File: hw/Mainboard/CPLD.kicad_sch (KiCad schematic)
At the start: 47 parts, among them J21 FPGA-P4, J22 Conn_02x15_Odd_Even, J23 FPGA_P2, J24 FPGA_P3, Q4 MMBT3904, SW5 CONFIG, U21 T8Q144C3, X1 50MHZ

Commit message: hw: wip
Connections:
- net ~{FPGA_PROG}: now reaches J22.22 (Pin_22)
- no-connect marks 31 -> 30
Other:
- note added: "AD7"
- note added: "~{FPGA_PROG} transitions low during CRESET (before ~{SS}) and returns high after ~{SS} deasserts."
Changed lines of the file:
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@@
   (no_connect (at 151.13 86.36))
   (no_connect (at 457.2 67.31))
-  (no_connect (at 457.2 64.77))
   (no_connect (at 457.2 87.63))
   (no_connect (at 457.2 85.09))
@@
     (stroke (width 0) (type default) (color 0 0 0 0))
   )
+  (wire (pts (xy 421.64 64.77) (xy 457.2 64.77))
+    (stroke (width 0) (type default) (color 0 0 0 0))
+  )
   (bus (pts (xy 337.82 54.61) (xy 337.82 57.15))
     (stroke (width 0) (type default) (color 0 0 0 0))
@@
   )
   (text "NSTATUS driven low on error" (at 435.61 163.83 0)
+    (effects (font (size 1.27 1.27)) (justify left bottom))
+  )
+  (text "~{FPGA_PROG} transitions low during CRESET\n(before ~{SS}) and returns high after ~{SS}\ndeasserts.\n"
+    (at 483.87 55.88 0)
     (effects (font (size 1.27 1.27)) (justify left bottom))
   )
@@
     (effects (font (size 1.27 1.27)) (justify right bottom))
   )
+  (text "AD7" (at 457.2 64.77 180)
+    (effects (font (size 1.27 1.27)) (justify right bottom))
+  )
   (text "BD3" (at 457.2 54.61 180)
     (effects (font (size 1.27 1.27)) (justify right bottom))
@@
     (effects (font (size 1.27 1.27)) (justify left))
   )
+  (hierarchical_label "~{FPGA_PROG}" (shape output) (at 421.64 64.77 180)
+    (effects (font (size 1.27 1.27)) (justify right))
+  )
   (hierarchical_label "VERT" (shape output) (at 386.08 105.41 90)

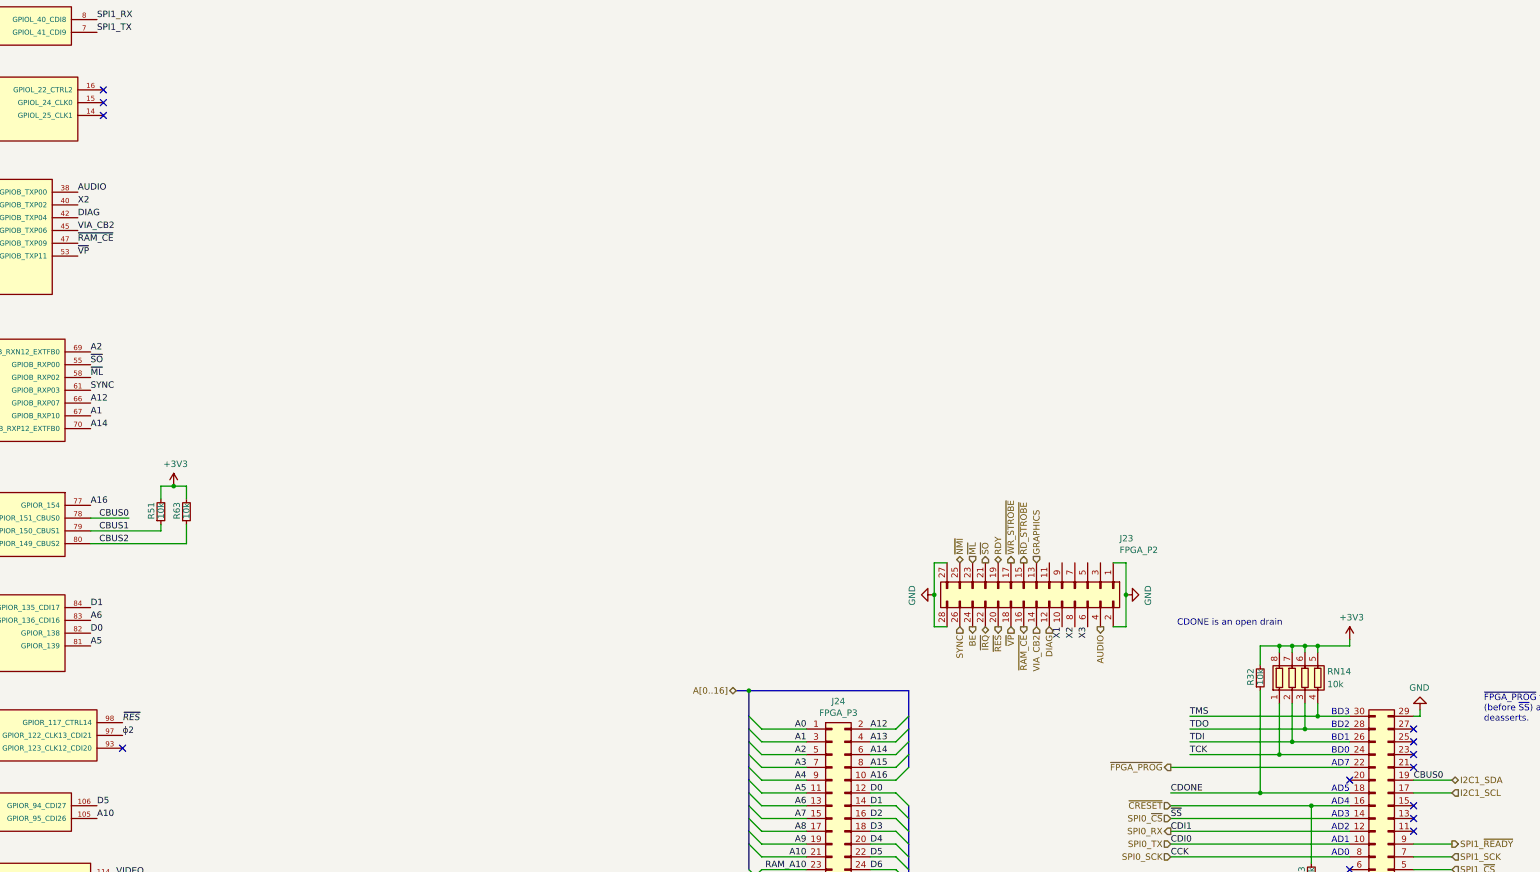
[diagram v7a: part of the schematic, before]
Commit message: hw: pull cbus0 high
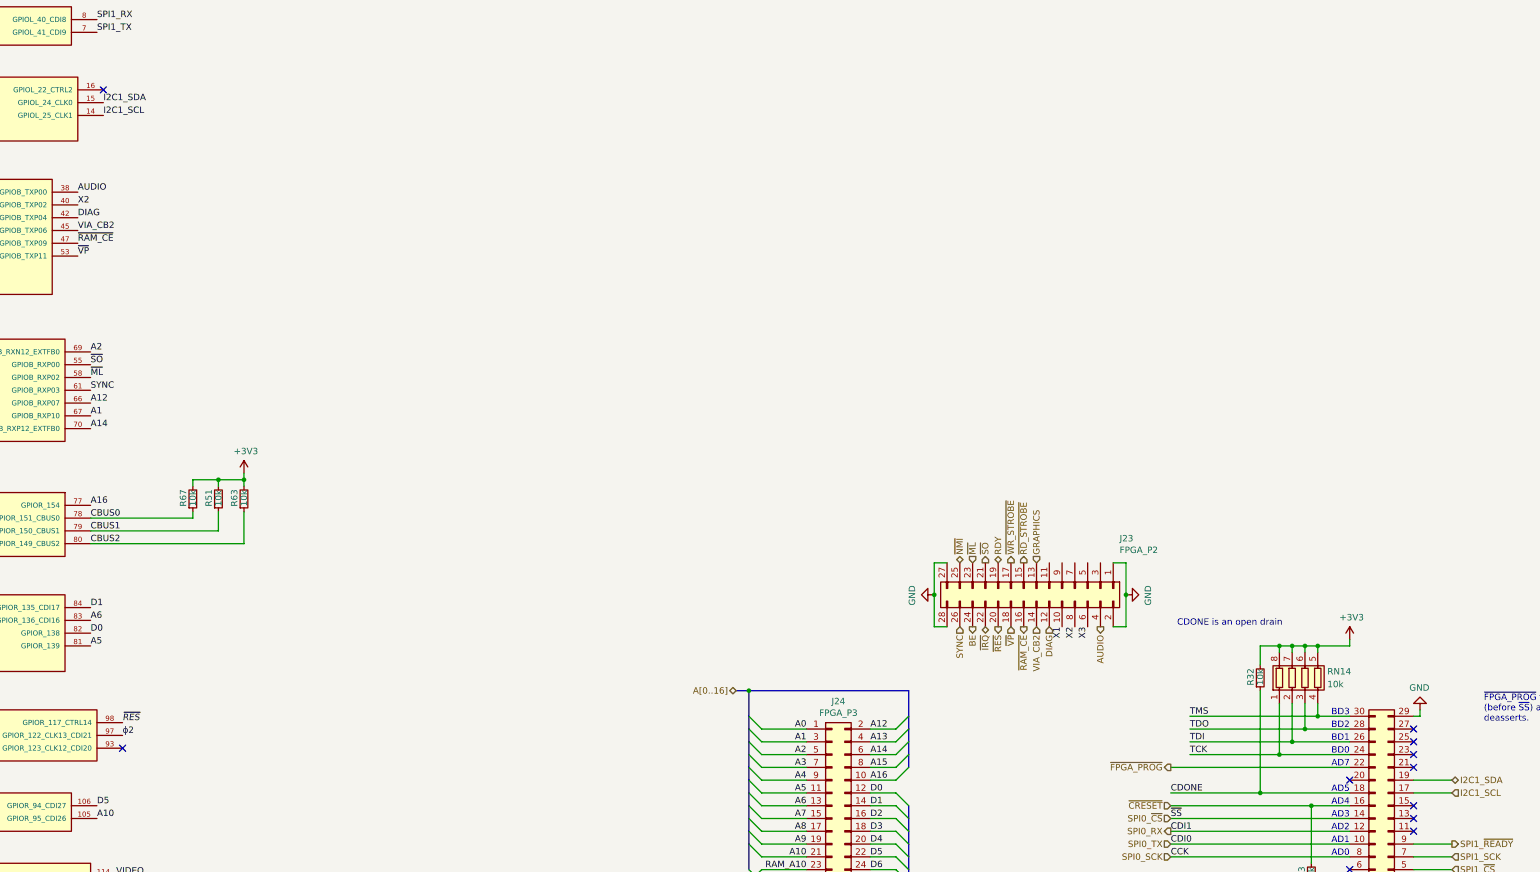
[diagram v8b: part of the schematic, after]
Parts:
- added R67: 10k, Resistor_SMD:R_0402_1005Metric, symbol Device:R_Small
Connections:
- net +3V3: now also R67.2
- net I2C1_SCL: now also U21.14 (GPIOL_25_CLK1)
- net I2C1_SDA: now also U21.15 (GPIOL_24_CLK0); no longer U21.78 (GPIOR_151_CBUS0)
- new net CBUS0: R67.1, U21.78 (GPIOR_151_CBUS0)
- no-connect marks 30 -> 28
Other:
- moved on the sheet: R51, R63
